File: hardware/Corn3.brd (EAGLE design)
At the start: 40.6 x 20.3 mm, 74 parts, among them IC1 STM32F10XCXT6, J1 JTAG-MINI, J4 PICOBLADE-UART-PORT, U3 AS1362, U4 DRV8301

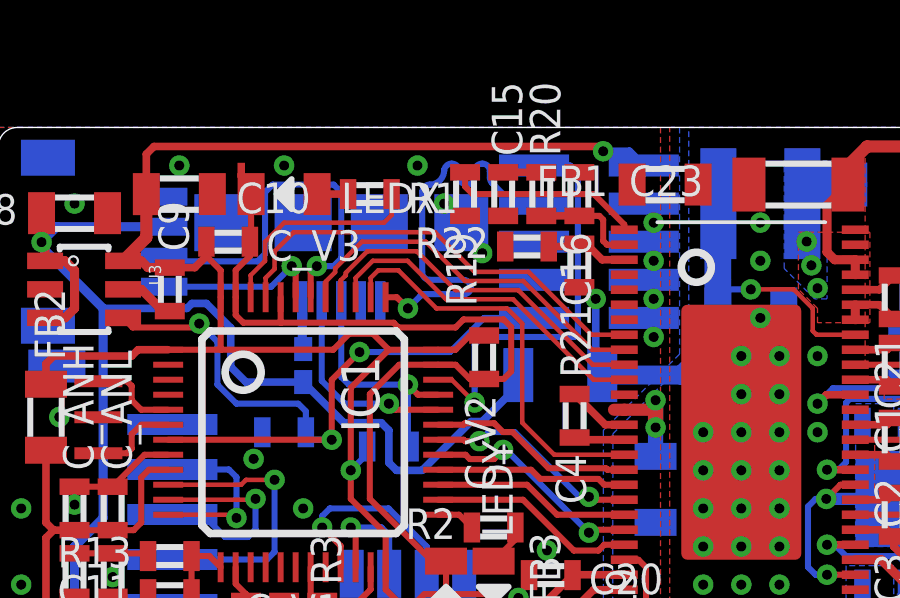
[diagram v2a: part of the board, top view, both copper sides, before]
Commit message: Start hardware v3.3. Unserpentine SWCLK trace (#30).
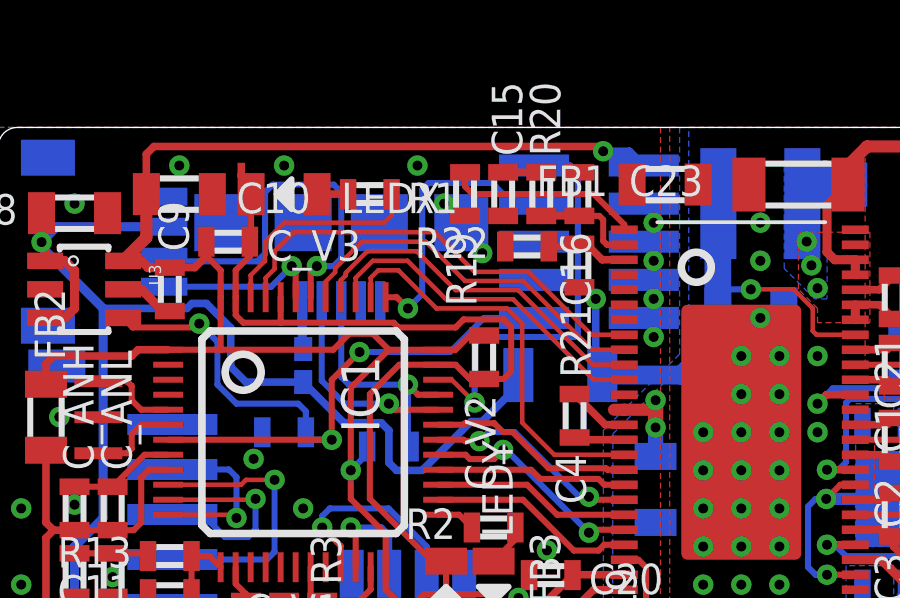
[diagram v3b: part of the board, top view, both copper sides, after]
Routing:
- net SWCLK: track 13.5 -> 9.16 mm
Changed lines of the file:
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@@
 <setting verticaltext="up"/>
 </settings>
-<grid distance="0.1" unitdist="inch" unit="inch" style="lines" multiple="1" display="no" altdistance="0.0125" altunitdist="inch" altunit="inch"/>
+<grid distance="100" unitdist="mil" unit="mil" style="lines" multiple="1" display="yes" altdistance="12.5" altunitdist="mil" altunit="mil"/>
 <layers>
 <layer number="1" name="Top" color="4" fill="1" visible="yes" active="yes"/>
@@
 <layer number="200" name="tLogo" color="15" fill="1" visible="no" active="yes"/>
 <layer number="201" name="bLogo" color="15" fill="1" visible="no" active="yes"/>
-<layer number="202" name="202bmp" color="3" fill="1" visible="no" active="no"/>
-<layer number="203" name="203bmp" color="4" fill="1" visible="no" active="yes"/>
+<layer number="202" name="202bmp" color="3" fill="1" visible="no" active="yes"/>
+<layer number="203" name="203bmp" color="5" fill="1" visible="no" active="yes"/>
 <layer number="204" name="204bmp" color="5" fill="10" visible="no" active="yes"/>
 <layer number="205" name="205bmp" color="6" fill="10" visible="no" active="yes"/>
@@
 <wire x1="15.0775" y1="11.91" x2="14.66" y2="11.91" width="0.1524" layer="1"/>
 <wire x1="15.875" y1="11.1506" x2="15.875" y2="11.148" width="0.1524" layer="1"/>
-<wire x1="15.113" y1="11.91" x2="15.875" y2="11.148" width="0.1524" layer="1"/>
+<wire x1="15.875" y1="11.148" x2="15.113" y2="11.91" width="0.1524" layer="1"/>
 <wire x1="15.113" y1="11.91" x2="14.66" y2="11.91" width="0.1524" layer="1"/>
 <wire x1="15.875" y1="11.1506" x2="15.875" y2="13.081" width="0.2032" layer="16"/>
@@
 <wire x1="13.28" y1="14.66" x2="13.6525" y2="14.2875" width="0.2032" layer="1"/>
 <via x="13.6525" y="14.2875" extent="1-16" drill="0.3302"/>
-<wire x1="13.6525" y1="14.2875" x2="14.05435625" y2="14.68935625" width="0.2032" layer="16"/>
-<wire x1="14.05435625" y1="14.68935625" x2="14.233959375" y2="14.76375" width="0.2032" layer="16" curve="-44.999295"/>
-<wire x1="14.233959375" y1="14.76375" x2="15.52575" y2="14.76375" width="0.2032" layer="16"/>
+<wire x1="13.6525" y1="14.2875" x2="14.12875" y2="14.76375" width="0.2032" layer="16"/>
 <wire x1="17.145" y1="17.78" x2="17.8562" y2="17.78" width="0.2032" layer="16"/>
 <wire x1="17.145" y1="17.78" x2="16.45739375" y2="18.46760625" width="0.2032" layer="16"/>
-<wire x1="16.45739375" y1="18.46760625" x2="16.383" y2="18.647209375" width="0.2032" layer="16" curve="-44.999295"/>
-<wire x1="16.383" y1="18.647209375" x2="16.383" y2="18.8595" width="0.2032" layer="16"/>
-<wire x1="16.383" y1="18.8595" x2="16.129" y2="19.1135" width="0.2032" layer="16" curve="90"/>
-<wire x1="16.129" y1="19.1135" x2="15.875" y2="18.8595" width="0.2032" layer="16" curve="90"/>
-<wire x1="15.875" y1="18.8595" x2="15.875" y2="18.669" width="0.2032" layer="16"/>
-<wire x1="15.875" y1="18.669" x2="15.621" y2="18.415" width="0.2032" layer="16" curve="-90"/>
-<wire x1="15.621" y1="18.415" x2="15.367" y2="18.669" width="0.2032" layer="16" curve="-90"/>
-<wire x1="15.367" y1="18.669" x2="15.367" y2="18.8595" width="0.2032" layer="16"/>
-<wire x1="15.367" y1="18.8595" x2="15.113" y2="19.1135" width="0.2032" layer="16" curve="90"/>
-<wire x1="15.113" y1="19.1135" x2="14.859" y2="18.8595" width="0.2032" layer="16" curve="90"/>
-<wire x1="14.859" y1="18.8595" x2="14.859" y2="18.89125" width="0.2032" layer="16"/>
-<wire x1="14.859" y1="18.89125" x2="14.38275" y2="18.415" width="0.2032" layer="16" curve="-90"/>
-<wire x1="14.12875" y1="18.161" x2="14.38275" y2="18.415" width="0.2032" layer="16" curve="-90"/>
-<wire x1="15.52575" y1="14.76375" x2="15.748" y2="14.986" width="0.2032" layer="16" curve="90"/>
-<wire x1="15.748" y1="14.986" x2="15.494" y2="15.24" width="0.2032" layer="16" curve="90"/>
-<wire x1="14.38275" y1="15.24" x2="15.494" y2="15.24" width="0.2032" layer="16"/>
-<wire x1="14.38275" y1="15.24" x2="14.12875" y2="15.494" width="0.2032" layer="16" curve="-90"/>
-<wire x1="14.12875" y1="18.161" x2="14.12875" y2="15.494" width="0.2032" layer="16"/>
+<wire x1="14.12875" y1="14.76375" x2="14.12875" y2="18.25625" width="0.2032" layer="16"/>
+<wire x1="14.12875" y1="18.25625" x2="14.34010625" y2="18.46760625" width="0.2032" layer="16"/>
+<wire x1="14.34010625" y1="18.46760625" x2="16.45739375" y2="18.46760625" width="0.2032" layer="16"/>
 </signal>
 <signal name="DRV_EN">

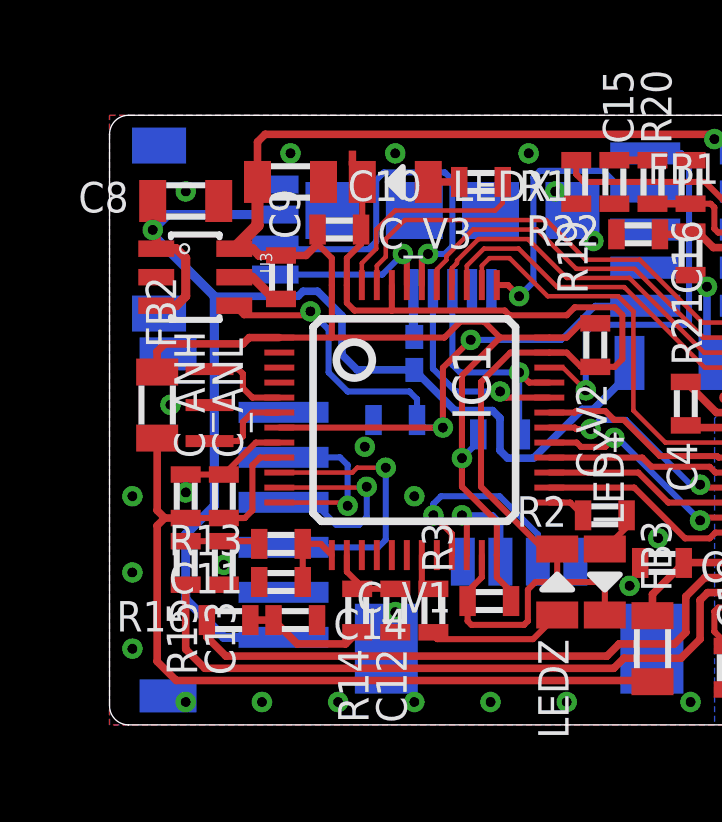
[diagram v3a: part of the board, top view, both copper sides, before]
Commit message: Fix reversed Hall connector (#31) and change pinout for flex port.
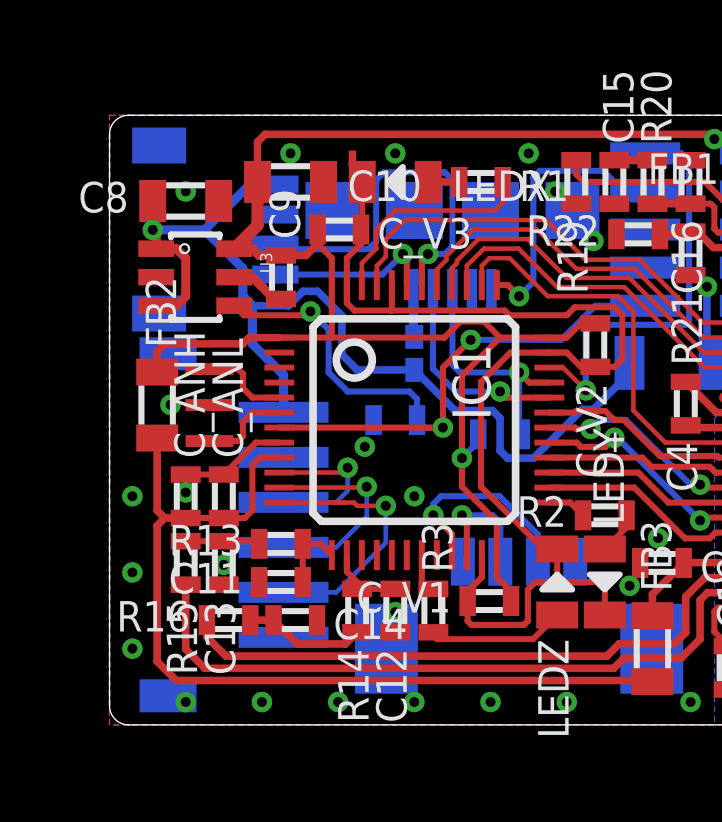
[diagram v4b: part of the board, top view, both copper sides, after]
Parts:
- JP1: value HALL_SENSOR_CONNECTOR_SM4A -> HALL-SENSOR-CONNECTOR_SM4A; device Xo-Connector:JST-S6B-ZR-SM4A -> Xo-Connector:JST_S6B-ZR-SM4A
- JP2: value FLEXIPORT_HORI -> FLEX-PORT_HORI
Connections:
- net +5V: now also JP2.4; no longer JP2.2
- net GND: now also JP2.3; no longer JP2.1
- net I2C_SCL: now also JP2.2; no longer JP2.3
- net I2C_SDA: now also JP2.1; no longer JP2.4
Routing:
- net +5V: track 45.9 -> 35.0 mm
- net HALL_A: track 9.53 -> 5.41 mm
- net HALL_C: track 5.93 -> 8.92 mm
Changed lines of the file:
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@@
 <element name="R22" library="dan-rcl" package="0603" value="10k" x="17.62125" y="16.35125" rot="R180"/>
 <element name="C23" library="dan-rcl" package="1206" value="4.7uF/50V" x="26.67" y="18.415" rot="R180"/>
-<element name="JP1" library="Xo-Connector" package="JST-S6B-ZR-SM4A" value="HALL_SENSOR_CONNECTOR_SM4A" x="0" y="6.6675" rot="MR270"/>
-<element name="JP2" library="Xo-Connector" package="JST_SM04B-SRSS" value="FLEXIPORT_HORI" x="0.9525" y="16.51" rot="MR270"/>
+<element name="JP1" library="Xo-Connector" package="JST_S6B-ZR-SM4A" value="HALL-SENSOR-CONNECTOR_SM4A" x="0" y="6.6675" rot="MR270"/>
+<element name="JP2" library="Xo-Connector" package="JST_SM04B-SRSS" value="FLEX-PORT_HORI" x="0.9525" y="16.51" rot="MR270"/>
 <element name="C17" library="dan-rcl" package="0603" value="1uF" x="23.495" y="12.065" rot="MR270"/>
 </elements>
@@
 <signal name="HALL_A">
 <contactref element="IC1" pad="10"/>
-<wire x1="5.66" y1="8.41" x2="8.0925" y2="8.41" width="0.1524" layer="1"/>
-<via x="9.2075" y="8.5725" extent="1-16" drill="0.3302"/>
+<wire x1="5.66" y1="8.41" x2="7.775" y2="8.41" width="0.1524" layer="1"/>
+<via x="7.9375" y="8.5725" extent="1-16" drill="0.3302"/>
 <contactref element="JP1" pad="4"/>
-<wire x1="8.0925" y1="8.41" x2="8.255" y2="8.5725" width="0.1524" layer="1"/>
-<wire x1="8.255" y1="8.5725" x2="9.2075" y2="8.5725" width="0.1524" layer="1"/>
-<wire x1="9.2075" y1="8.5725" x2="9.2075" y2="6.1715" width="0.2032" layer="16"/>
-<wire x1="9.2075" y1="6.1715" x2="8.9535" y2="5.9175" width="0.2032" layer="16"/>
-<wire x1="8.9535" y1="5.9175" x2="5.8" y2="5.9175" width="0.2032" layer="16"/>
+<wire x1="7.775" y1="8.41" x2="7.9375" y2="8.5725" width="0.1524" layer="1"/>
+<wire x1="7.9375" y1="8.5725" x2="7.9375" y2="7.7985" width="0.1524" layer="16"/>
+<wire x1="7.9375" y1="7.7985" x2="7.5565" y2="7.4175" width="0.1524" layer="16"/>
+<wire x1="7.5565" y1="7.4175" x2="5.8" y2="7.4175" width="0.1524" layer="16"/>
 </signal>
 <signal name="HALL_B">
@@
 <wire x1="5.66" y1="7.91" x2="8.545" y2="7.91" width="0.1524" layer="1"/>
 <wire x1="8.545" y1="7.91" x2="8.5725" y2="7.9375" width="0.1524" layer="1"/>
-<wire x1="8.5725" y1="7.9375" x2="8.5725" y2="6.9215" width="0.2032" layer="16"/>
-<wire x1="8.5725" y1="6.9215" x2="8.3185" y2="6.6675" width="0.2032" layer="16"/>
-<wire x1="8.3185" y1="6.6675" x2="7.5565" y2="6.6675" width="0.2032" layer="16"/>
-<wire x1="7.5565" y1="6.6675" x2="6.8065" y2="7.4175" width="0.2032" layer="16"/>
-<wire x1="6.8065" y1="7.4175" x2="5.8" y2="7.4175" width="0.2032" layer="16"/>
+<wire x1="8.5725" y1="7.9375" x2="8.5725" y2="6.9335" width="0.1524" layer="16"/>
+<wire x1="8.5725" y1="6.9335" x2="7.5565" y2="5.9175" width="0.1524" layer="16"/>
+<wire x1="7.5565" y1="5.9175" x2="5.8" y2="5.9175" width="0.1524" layer="16"/>
 </signal>
 <signal name="HALL_C">
 <contactref element="IC1" pad="12"/>
-<wire x1="5.66" y1="7.41" x2="7.83" y2="7.41" width="0.1524" layer="1"/>
-<via x="7.9375" y="7.3025" extent="1-16" drill="0.3302"/>
+<wire x1="5.66" y1="7.41" x2="7.62" y2="7.41" width="0.1524" layer="1"/>
+<via x="9.2075" y="7.3025" extent="1-16" drill="0.3302"/>
 <contactref element="JP1" pad="2"/>
-<wire x1="7.83" y1="7.41" x2="7.9375" y2="7.3025" width="0.1524" layer="1"/>
-<wire x1="7.9375" y1="7.3025" x2="7.9375" y2="8.6635" width="0.2032" layer="16"/>
-<wire x1="7.9375" y1="8.6635" x2="7.6835" y2="8.9175" width="0.2032" layer="16"/>
-<wire x1="7.6835" y1="8.9175" x2="5.8" y2="8.9175" width="0.2032" layer="16"/>
+<wire x1="7.62" y1="7.41" x2="7.83" y2="7.41" width="0.1524" layer="1"/>
+<wire x1="8.255" y1="7.3025" x2="9.2075" y2="7.3025" width="0.1524" layer="1"/>
+<wire x1="8.255" y1="7.3025" x2="8.1475" y2="7.41" width="0.1524" layer="1"/>
+<wire x1="8.1475" y1="7.41" x2="7.83" y2="7.41" width="0.1524" layer="1"/>
+<wire x1="9.2075" y1="7.3025" x2="9.2075" y2="6.0685" width="0.1524" layer="16"/>
+<wire x1="9.2075" y1="6.0685" x2="7.5565" y2="4.4175" width="0.1524" layer="16"/>
+<wire x1="7.5565" y1="4.4175" x2="5.8" y2="4.4175" width="0.1524" layer="16"/>
 </signal>
 <signal name="PWM_C">
@@
 <contactref element="C16" pad="1"/>
 <contactref element="R22" pad="2"/>
-<contactref element="JP1" pad="1"/>
-<contactref element="JP1" pad="TAB2"/>
-<contactref element="JP1" pad="TAB1"/>
 <contactref element="R19" pad="2"/>
-<contactref element="JP2" pad="TAB2"/>
-<contactref element="JP2" pad="TAB1"/>
-<contactref element="JP2" pad="1"/>
 <via x="19.3675" y="0.762" extent="1-16" drill="0.3302" shape="octagon"/>
 <via x="18.288" y="6.223" extent="1-16" drill="0.3302" shape="octagon"/>
@@
 <via x="3.81" y="5.334" extent="1-16" drill="0.3302" shape="octagon"/>
 <via x="17.3355" y="4.6355" extent="1-16" drill="0.3302" shape="octagon"/>
+<contactref element="JP2" pad="TAB2"/>
+<contactref element="JP2" pad="TAB1"/>
+<contactref element="JP2" pad="3"/>
+<contactref element="JP1" pad="1"/>
+<contactref element="JP1" pad="TAB2"/>
+<contactref element="JP1" pad="TAB1"/>
 </signal>
 <signal name="+3V3_FILT">
@@
 <contactref element="D1" pad="C"/>
 <contactref element="F1" pad="2"/>
-<contactref element="JP1" pad="6"/>
-<contactref element="JP2" pad="2"/>
 <wire x1="1.5574" y1="15.8725" x2="1.5574" y2="16.38135" width="0.3048" layer="1"/>
 <wire x1="1.5574" y1="16.38135" x2="1.44" y2="16.49875" width="0.3048" layer="1"/>
 <wire x1="1.44" y1="16.49875" x2="1.44" y2="17.4625" width="0.3048" layer="1"/>
 <via x="1.44" y="16.49875" extent="1-16" drill="0.3302"/>
-<wire x1="1.44" y1="16.49875" x2="1.95125" y2="17.01" width="0.3048" layer="16"/>
-<wire x1="1.95125" y1="17.01" x2="5.5275" y2="17.01" width="0.3048" layer="16"/>
-<wire x1="1.44" y1="16.49875" x2="1.44" y2="16.34" width="0.3048" layer="16"/>
-<wire x1="1.44" y1="16.34" x2="3.4925" y2="14.2875" width="0.3048" layer="16"/>
-<wire x1="2.54" y1="6.35" x2="2.54" y2="4.1875" width="0.3048" layer="16"/>
-<wire x1="2.54" y1="4.1875" x2="3.81" y2="2.9175" width="0.3048" layer="16"/>
-<wire x1="3.81" y1="2.9175" x2="5.8" y2="2.9175" width="0.3048" layer="16"/>
-<wire x1="3.4925" y1="14.2875" x2="6.2865" y2="14.2875" width="0.254" layer="16"/>
-<wire x1="6.2865" y1="14.2875" x2="6.4516" y2="14.4526" width="0.254" layer="16"/>
+<wire x1="4.7625" y1="13.97" x2="5.969" y2="13.97" width="0.254" layer="16"/>
+<wire x1="5.969" y1="13.97" x2="6.4516" y2="14.4526" width="0.254" layer="16"/>
 <wire x1="6.4516" y1="14.4526" x2="6.9342" y2="14.4526" width="0.254" layer="16"/>
 <wire x1="6.9342" y1="14.4526" x2="7.747" y2="13.6398" width="0.254" layer="16"/>
@@
 <wire x1="16.129" y1="10.5156" x2="17.3325" y2="11.7191" width="0.254" layer="16"/>
 <wire x1="17.3325" y1="11.7191" x2="17.3325" y2="12.065" width="0.254" layer="16"/>
-<wire x1="3.4925" y1="14.2875" x2="3.4925" y2="7.3025" width="0.3048" layer="16"/>
-<wire x1="3.4925" y1="7.3025" x2="2.54" y2="6.35" width="0.3048" layer="16"/>
+<contactref element="JP2" pad="4"/>
+<wire x1="4.675" y1="18.01" x2="5.5275" y2="18.01" width="0.3048" layer="16"/>
+<contactref element="JP1" pad="6"/>
+<wire x1="4.445" y1="15.2175" x2="4.445" y2="14.2875" width="0.3048" layer="16"/>
+<wire x1="4.445" y1="14.2875" x2="4.7625" y2="13.97" width="0.3048" layer="16"/>
+<wire x1="4.7625" y1="13.97" x2="4.7625" y2="12.7" width="0.3048" layer="16"/>
+<wire x1="4.7625" y1="12.7" x2="5.8" y2="11.6625" width="0.3048" layer="16"/>
+<wire x1="5.8" y1="11.6625" x2="5.8" y2="10.4175" width="0.3048" layer="16"/>
+<wire x1="4.675" y1="18.01" x2="3.16375" y2="16.49875" width="0.3048" layer="16"/>
+<wire x1="3.16375" y1="16.49875" x2="1.44" y2="16.49875" width="0.3048" layer="16"/>
+<wire x1="3.16375" y1="16.49875" x2="4.445" y2="15.2175" width="0.3048" layer="16"/>
 </signal>
 <signal name="N$8">
@@
 <signal name="I2C_SCL">
 <contactref element="IC1" pad="42"/>
-<contactref element="JP2" pad="3"/>
+<contactref element="JP2" pad="2"/>
 <via x="10.6172" y="15.6972" extent="1-16" drill="0.3302"/>
 <wire x1="6.05155" y1="15.85595" x2="5.8975" y2="16.01" width="0.2032" layer="16"/>
@@
 <signal name="I2C_SDA">
 <contactref element="IC1" pad="43"/>
-<contactref element="JP2" pad="4"/>
+<contactref element="JP2" pad="1"/>
 <wire x1="9.91" y1="14.66" x2="9.91" y2="15.5662" width="0.2032" layer="1"/>
 <via x="9.779" y="15.6972" extent="1-16" drill="0.3302"/>
